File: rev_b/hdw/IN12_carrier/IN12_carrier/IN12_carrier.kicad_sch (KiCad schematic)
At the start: 0 parts

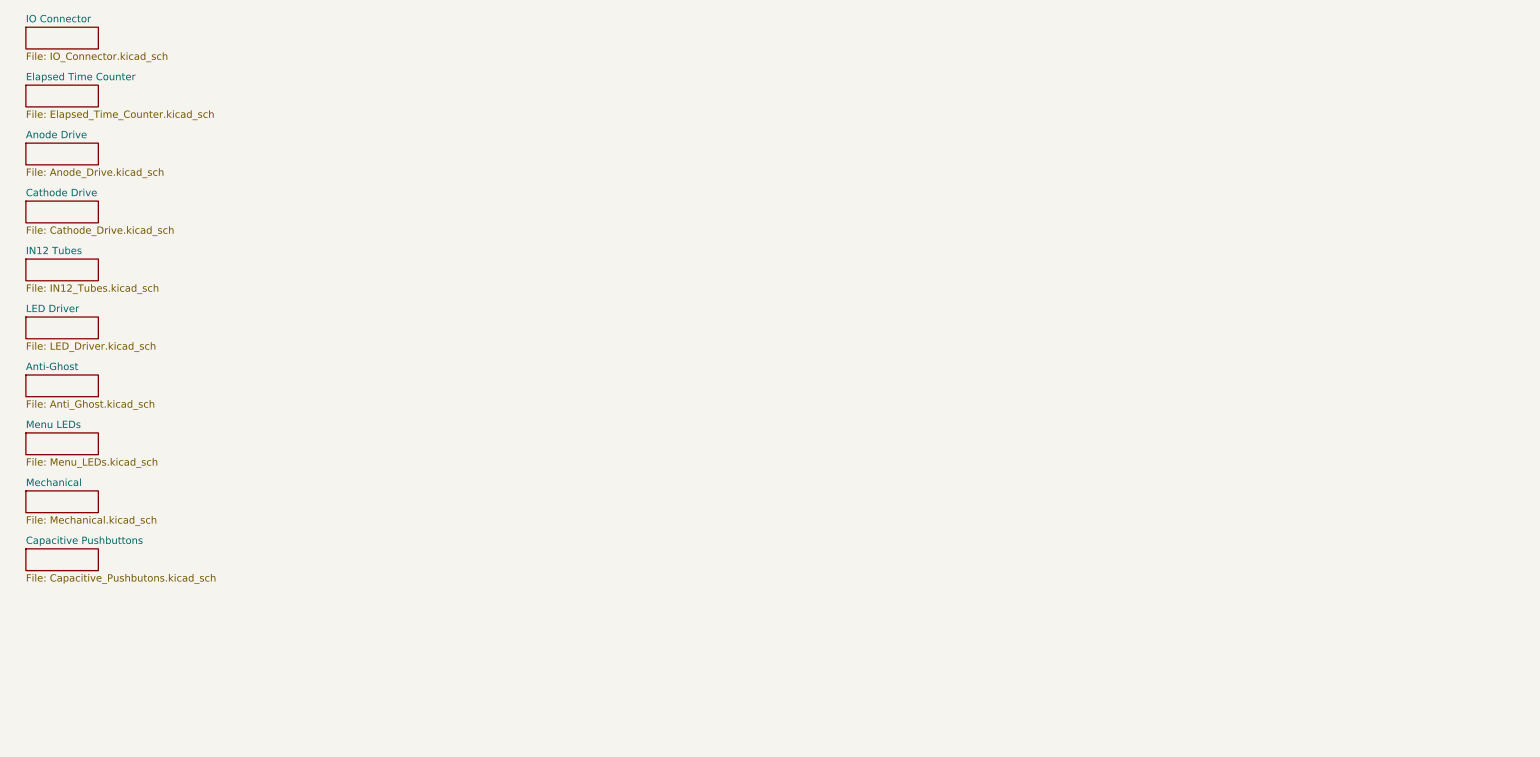
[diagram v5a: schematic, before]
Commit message: added BOM for IN12 carrier, finished routing, some schematic tweaks, adjusted design rules for ERC
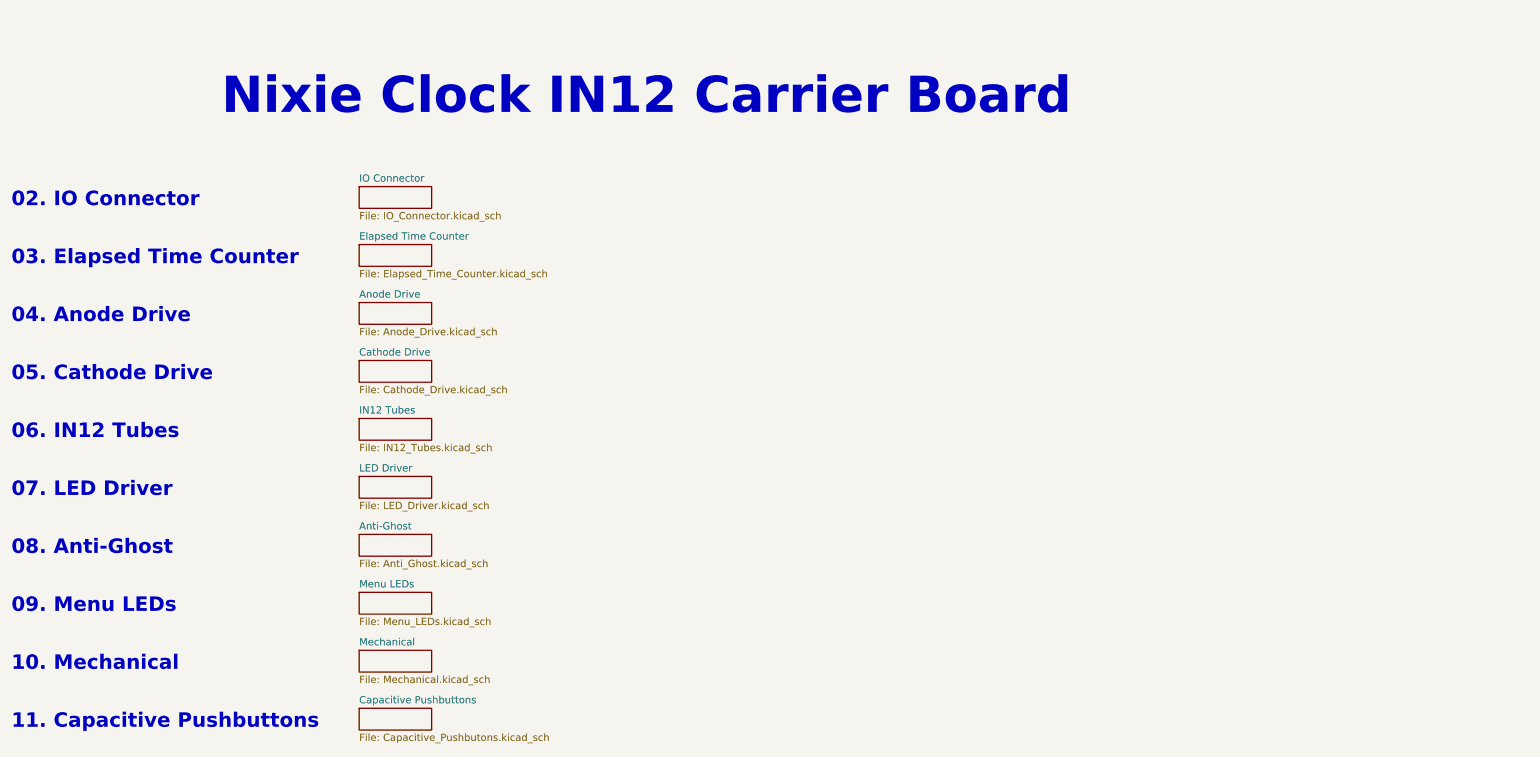
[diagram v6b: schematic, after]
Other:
- note added: "02. IO Connector"
- note added: "03. Elapsed Time Counter"
- note added: "04. Anode Drive"
- note added: "05. Cathode Drive"
- note added: "06. IN12 Tubes"
- note added: "07. LED Driver"
- note added: "08. Anti-Ghost"
- note added: "09. Menu LEDs"
- note added: "10. Mechanical"
- note added: "11. Capacitive Pushbuttons"
- note added: "Nixie Clock IN12 Carrier Board"
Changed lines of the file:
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@@
     (company "Drew Maatman")
   )
-  (sheet (at 19.05 107.95) (size 12.7 3.81) (fields_autoplaced)
+  (text "05. Cathode Drive" (at 16.51 78.74 0)
+    (effects (font (face "Courier New") (size 2.54 2.54) (thickness 0.508) bold) (justify left bottom))
+  )
+  (text "04. Anode Drive" (at 16.51 68.58 0)
+    (effects (font (face "Courier New") (size 2.54 2.54) (thickness 0.508) bold) (justify left bottom))
+  )
+  (text "11. Capacitive Pushbuttons" (at 16.51 139.7 0)
+    (effects (font (face "Courier New") (size 2.54 2.54) (thickness 0.508) bold) (justify left bottom))
+  )
+  (text "09. Menu LEDs" (at 16.51 119.38 0)
+    (effects (font (face "Courier New") (size 2.54 2.54) (thickness 0.508) bold) (justify left bottom))
+  )
+  (text "10. Mechanical" (at 16.51 129.54 0)
+    (effects (font (face "Courier New") (size 2.54 2.54) (thickness 0.508) bold) (justify left bottom))
+  )
+  (text "07. LED Driver" (at 16.51 99.06 0)
+    (effects (font (face "Courier New") (size 2.54 2.54) (thickness 0.508) bold) (justify left bottom))
+  )
+  (text "02. IO Connector" (at 16.51 48.26 0)
+    (effects (font (face "Courier New") (size 2.54 2.54) (thickness 0.508) bold) (justify left bottom))
+  )
+  (text "06. IN12 Tubes" (at 16.51 88.9 0)
+    (effects (font (face "Courier New") (size 2.54 2.54) (thickness 0.508) bold) (justify left bottom))
+  )
+  (text "Nixie Clock IN12 Carrier Board" (at 53.34 32.385 0)
+    (effects (font (face "Courier New") (size 6.35 6.35) (thickness 1.27) bold) (justify left bottom))
+  )
+  (text "03. Elapsed Time Counter" (at 16.51 58.42 0)
+    (effects (font (face "Courier New") (size 2.54 2.54) (thickness 0.508) bold) (justify left bottom))
+  )
+  (text "08. Anti-Ghost" (at 16.51 109.22 0)
+    (effects (font (face "Courier New") (size 2.54 2.54) (thickness 0.508) bold) (justify left bottom))
+  )
+  (sheet (at 77.47 135.89) (size 12.7 3.81) (fields_autoplaced)
     (stroke (width 0.1524) (type solid))
     (fill (color 0 0 0 0.0000))
-    (property "Sheetname" "Capacitive Pushbuttons" (at 19.05 107.2384 0)
+    (property "Sheetname" "Capacitive Pushbuttons" (at 77.47 135.1784 0)
       (effects (font (size 1.27 1.27)) (justify left bottom))
     )
-    (property "Sheetfile" "Capacitive_Pushbutons.kicad_sch" (at 19.05 112.3446 0)
+    (property "Sheetfile" "Capacitive_Pushbutons.kicad_sch" (at 77.47 140.2846 0)
       (effects (font (size 1.27 1.27)) (justify left top))
     )
@@
     )
   )
-  (sheet (at 19.05 46.99) (size 12.7 3.81) (fields_autoplaced)
+  (sheet (at 77.47 74.93) (size 12.7 3.81) (fields_autoplaced)
     (stroke (width 0.1524) (type solid))
     (fill (color 0 0 0 0.0000))
-    (property "Sheetname" "Cathode Drive" (at 19.05 46.2784 0)
+    (property "Sheetname" "Cathode Drive" (at 77.47 74.2184 0)
       (effects (font (size 1.27 1.27)) (justify left bottom))
     )
-    (property "Sheetfile" "Cathode_Drive.kicad_sch" (at 19.05 51.3846 0)
+    (property "Sheetfile" "Cathode_Drive.kicad_sch" (at 77.47 79.3246 0)
       (effects (font (size 1.27 1.27)) (justify left top))
     )
@@
     )
   )
-  (sheet (at 19.05 57.15) (size 12.7 3.81) (fields_autoplaced)
+  (sheet (at 77.47 85.09) (size 12.7 3.81) (fields_autoplaced)
     (stroke (width 0.1524) (type solid))
     (fill (color 0 0 0 0.0000))
-    (property "Sheetname" "IN12 Tubes" (at 19.05 56.4384 0)
+    (property "Sheetname" "IN12 Tubes" (at 77.47 84.3784 0)
       (effects (font (size 1.27 1.27)) (justify left bottom))
     )
-    (property "Sheetfile" "IN12_Tubes.kicad_sch" (at 19.05 61.5446 0)
+    (property "Sheetfile" "IN12_Tubes.kicad_sch" (at 77.47 89.4846 0)
       (effects (font (size 1.27 1.27)) (justify left top))
     )
@@
     )
   )
-  (sheet (at 19.05 97.79) (size 12.7 3.81) (fields_autoplaced)
+  (sheet (at 77.47 125.73) (size 12.7 3.81) (fields_autoplaced)
     (stroke (width 0.1524) (type solid))
     (fill (color 0 0 0 0.0000))
-    (property "Sheetname" "Mechanical" (at 19.05 97.0784 0)
+    (property "Sheetname" "Mechanical" (at 77.47 125.0184 0)
       (effects (font (size 1.27 1.27)) (justify left bottom))
     )
-    (property "Sheetfile" "Mechanical.kicad_sch" (at 19.05 102.1846 0)
+    (property "Sheetfile" "Mechanical.kicad_sch" (at 77.47 130.1246 0)
       (effects (font (size 1.27 1.27)) (justify left top))
     )
@@
     )
   )
-  (sheet (at 19.05 16.51) (size 12.7 3.81) (fields_autoplaced)
+  (sheet (at 77.47 44.45) (size 12.7 3.81) (fields_autoplaced)
     (stroke (width 0.1524) (type solid))
     (fill (color 0 0 0 0.0000))
-    (property "Sheetname" "IO Connector" (at 19.05 15.7984 0)
+    (property "Sheetname" "IO Connector" (at 77.47 43.7384 0)
       (effects (font (size 1.27 1.27)) (justify left bottom))
     )
-    (property "Sheetfile" "IO_Connector.kicad_sch" (at 19.05 20.9046 0)
+    (property "Sheetfile" "IO_Connector.kicad_sch" (at 77.47 48.8446 0)
       (effects (font (size 1.27 1.27)) (justify left top))
     )
@@
     )
   )
-  (sheet (at 19.05 87.63) (size 12.7 3.81) (fields_autoplaced)
+  (sheet (at 77.47 115.57) (size 12.7 3.81) (fields_autoplaced)
     (stroke (width 0.1524) (type solid))
     (fill (color 0 0 0 0.0000))
-    (property "Sheetname" "Menu LEDs" (at 19.05 86.9184 0)
+    (property "Sheetname" "Menu LEDs" (at 77.47 114.8584 0)
       (effects (font (size 1.27 1.27)) (justify left bottom))
     )
-    (property "Sheetfile" "Menu_LEDs.kicad_sch" (at 19.05 92.0246 0)
+    (property "Sheetfile" "Menu_LEDs.kicad_sch" (at 77.47 119.9646 0)
       (effects (font (size 1.27 1.27)) (justify left top))
     )
@@
     )
   )
-  (sheet (at 19.05 26.67) (size 12.7 3.81) (fields_autoplaced)
+  (sheet (at 77.47 54.61) (size 12.7 3.81) (fields_autoplaced)
     (stroke (width 0.1524) (type solid))
     (fill (color 0 0 0 0.0000))
-    (property "Sheetname" "Elapsed Time Counter" (at 19.05 25.9584 0)
+    (property "Sheetname" "Elapsed Time Counter" (at 77.47 53.8984 0)
       (effects (font (size 1.27 1.27)) (justify left bottom))
     )
-    (property "Sheetfile" "Elapsed_Time_Counter.kicad_sch" (at 19.05 31.0646 0)
+    (property "Sheetfile" "Elapsed_Time_Counter.kicad_sch" (at 77.47 59.0046 0)
       (effects (font (size 1.27 1.27)) (justify left top))
     )
@@
     )
   )
-  (sheet (at 19.05 36.83) (size 12.7 3.81) (fields_autoplaced)
+  (sheet (at 77.47 64.77) (size 12.7 3.81) (fields_autoplaced)
     (stroke (width 0.1524) (type solid))
     (fill (color 0 0 0 0.0000))
-    (property "Sheetname" "Anode Drive" (at 19.05 36.1184 0)
+    (property "Sheetname" "Anode Drive" (at 77.47 64.0584 0)
       (effects (font (size 1.27 1.27)) (justify left bottom))
     )
-    (property "Sheetfile" "Anode_Drive.kicad_sch" (at 19.05 41.2246 0)
+    (property "Sheetfile" "Anode_Drive.kicad_sch" (at 77.47 69.1646 0)
       (effects (font (size 1.27 1.27)) (justify left top))
     )
@@
     )
   )
-  (sheet (at 19.05 67.31) (size 12.7 3.81) (fields_autoplaced)
+  (sheet (at 77.47 95.25) (size 12.7 3.81) (fields_autoplaced)
     (stroke (width 0.1524) (type solid))
     (fill (color 0 0 0 0.0000))
-    (property "Sheetname" "LED Driver" (at 19.05 66.5984 0)
+    (property "Sheetname" "LED Driver" (at 77.47 94.5384 0)
       (effects (font (size 1.27 1.27)) (justify left bottom))
     )
-    (property "Sheetfile" "LED_Driver.kicad_sch" (at 19.05 71.7046 0)
+    (property "Sheetfile" "LED_Driver.kicad_sch" (at 77.47 99.6446 0)
       (effects (font (size 1.27 1.27)) (justify left top))
     )
@@
     )
   )
-  (sheet (at 19.05 77.47) (size 12.7 3.81) (fields_autoplaced)
+  (sheet (at 77.47 105.41) (size 12.7 3.81) (fields_autoplaced)
     (stroke (width 0.1524) (type solid))
     (fill (color 0 0 0 0.0000))
-    (property "Sheetname" "Anti-Ghost" (at 19.05 76.7584 0)
+    (property "Sheetname" "Anti-Ghost" (at 77.47 104.6984 0)
       (effects (font (size 1.27 1.27)) (justify left bottom))
     )
-    (property "Sheetfile" "Anti_Ghost.kicad_sch" (at 19.05 81.8646 0)
+    (property "Sheetfile" "Anti_Ghost.kicad_sch" (at 77.47 109.8046 0)
       (effects (font (size 1.27 1.27)) (justify left top))
     )
